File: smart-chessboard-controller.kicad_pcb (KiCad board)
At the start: 4 copper layers, 89.8 x 92.5 mm, 75 parts, among them J1 USB_C_Receptacle_USB2.0, J2 Micro_SD_Card_Det_Hirose_DM3C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, J3 Conn_02x03_Odd_Even, J4 Conn_01x12_MountingPin, J5 NX3224T024, J6 Conn_01x05, J7 Conn_01x05, J8 Conn_01x05, J9 Conn_01x05, Q1 S8050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

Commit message: update USB-C footprint to through hole
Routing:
- net 5V: track 137.6 -> 136.2 mm
- net /W_MOVE: track 38.6 -> 39.7 mm
- net GND: vias 17 -> 26

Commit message: fix pin assignment for black clock connector
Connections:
- J6 pad 2: /SCL_DB -> /SDA_DB
- J6 pad 3: /SDA_DB -> /SCL_DB
- J9 pad 2: /SCL_DBC -> /SDA_DBC
- J9 pad 3: /SDA_DBC -> /SCL_DBC
- R12 pad 2: /SDA_DBC -> /SCL_DBC
- R16 pad 2: /SCL_DBC -> /SDA_DBC
- U5 pad 8: /SCL_DBC -> /SDA_DBC
- U5 pad 9: /SDA_DBC -> /SCL_DBC
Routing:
- net /SDA_DBC: track 21.0 -> 23.4 mm
- net /SCL_DBC: track 23.4 -> 21.0 mm
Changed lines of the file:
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@@
   (title_block
     (title "Smart Chessboard Controller")
-    (date "2022-11-25")
-    (rev "B")
+    (date "2022-12-07")
+    (rev "C")
     (company "Butler Electronics")
   )
@@
       (net 85 "unconnected-(U5-Pad7)") (pinfunction "SC1") (pintype "output+no_connect"))
     (pad "8" smd roundrect (at -2.8625 0.975 90) (size 1.475 0.4) (layers "F.Cu" "F.Paste" "F.Mask") (roundrect_rratio 0.25)
-      (net 99 "/SCL_DBC") (pinfunction "SD2") (pintype "bidirectional"))
+      (net 98 "/SDA_DBC") (pinfunction "SD2") (pintype "bidirectional"))
     (pad "9" smd roundrect (at -2.8625 1.625 90) (size 1.475 0.4) (layers "F.Cu" "F.Paste" "F.Mask") (roundrect_rratio 0.25)
-      (net 98 "/SDA_DBC") (pinfunction "SC2") (pintype "output"))
+      (net 99 "/SCL_DBC") (pinfunction "SC2") (pintype "output"))
     (pad "10" smd roundrect (at -2.8625 2.275 90) (size 1.475 0.4) (layers "F.Cu" "F.Paste" "F.Mask") (roundrect_rratio 0.25)
       (net 96 "/SDA_DWC") (pinfunction "SD3") (pintype "bidirectional"))
@@
       (net 1 "3V3") (pintype "passive"))
     (pad "2" smd roundrect (at 0.825 0 180) (size 0.8 0.95) (layers "F.Cu" "F.Paste" "F.Mask") (roundrect_rratio 0.25)
-      (net 99 "/SCL_DBC") (pintype "passive"))
+      (net 98 "/SDA_DBC") (pintype "passive"))
     (model "${KICAD6_3DMODEL_DIR}/Resistor_SMD.3dshapes/R_0603_1608Metric.wrl"
       (offset (xyz 0 0 0))
@@
       (net 1 "3V3") (pinfunction "Pin_1") (pintype "passive"))
     (pad "2" thru_hole oval (at 2 0) (size 1.2 1.75) (drill 0.75) (layers *.Cu *.Mask)
-      (net 99 "/SCL_DBC") (pinfunction "Pin_2") (pintype "passive"))
+      (net 98 "/SDA_DBC") (pinfunction "Pin_2") (pintype "passive"))
     (pad "3" thru_hole oval (at 4 0) (size 1.2 1.75) (drill 0.75) (layers *.Cu *.Mask)
-      (net 98 "/SDA_DBC") (pinfunction "Pin_3") (pintype "passive"))
+      (net 99 "/SCL_DBC") (pinfunction "Pin_3") (pintype "passive"))
     (pad "4" thru_hole oval (at 6 0) (size 1.2 1.75) (drill 0.75) (layers *.Cu *.Mask)
       (net 38 "/B_MOVE") (pinfunction "Pin_4") (pintype "passive"))
@@
       (net 1 "3V3") (pintype "passive"))
     (pad "2" smd roundrect (at 0.825 0 180) (size 0.8 0.95) (layers "F.Cu" "F.Paste" "F.Mask") (roundrect_rratio 0.25)
-      (net 98 "/SDA_DBC") (pintype "passive"))
+      (net 99 "/SCL_DBC") (pintype "passive"))
     (model "${KICAD6_3DMODEL_DIR}/Resistor_SMD.3dshapes/R_0603_1608Metric.wrl"
       (offset (xyz 0 0 0))
@@
       (net 103 "+3V3") (pinfunction "Pin_1") (pintype "passive"))
     (pad "2" thru_hole oval (at 2 0 180) (size 1.2 1.75) (drill 0.75) (layers *.Cu *.Mask)
-      (net 32 "/SCL_DB") (pinfunction "Pin_2") (pintype "passive"))
+      (net 31 "/SDA_DB") (pinfunction "Pin_2") (pintype "passive"))
     (pad "3" thru_hole oval (at 4 0 180) (size 1.2 1.75) (drill 0.75) (layers *.Cu *.Mask)
-      (net 31 "/SDA_DB") (pinfunction "Pin_3") (pintype "passive"))
+      (net 32 "/SCL_DB") (pinfunction "Pin_3") (pintype "passive"))
     (pad "4" thru_hole oval (at 6 0 180) (size 1.2 1.75) (drill 0.75) (layers *.Cu *.Mask)
       (net 33 "/B_MOVE_BTN") (pinfunction "Pin_4") (pintype "passive"))
@@
   (segment (start 112.52 94.994) (end 108.841 91.315) (width 0.2) (layer "F.Cu") (net 97))
   (segment (start 112.586 89.027) (end 112.268 89.027) (width 0.25) (layer "F.Cu") (net 97))
-  (segment (start 112.586 85.979) (end 109.855 85.979) (width 0.25) (layer "F.Cu") (net 98))
-  (segment (start 107.541 92.103) (end 105.664 93.98) (width 0.25) (layer "F.Cu") (net 98))
-  (segment (start 109.855 85.979) (end 107.541 88.293) (width 0.25) (layer "F.Cu") (net 98))
-  (segment (start 99.312 95.506) (end 99.312 97.08) (width 0.25) (layer "F.Cu") (net 98))
-  (segment (start 107.541 89.6035) (end 107.541 92.103) (width 0.25) (layer "F.Cu") (net 98))
-  (segment (start 100.838 93.98) (end 99.312 95.506) (width 0.25) (layer "F.Cu") (net 98))
-  (segment (start 105.664 93.98) (end 100.838 93.98) (width 0.25) (layer "F.Cu") (net 98))
-  (segment (start 107.541 88.293) (end 107.541 89.6035) (width 0.25) (layer "F.Cu") (net 98))
-  (segment (start 97.312 95.728) (end 97.312 97.08) (width 0.25) (layer "F.Cu") (net 99))
-  (segment (start 112.586 84.455) (end 111.887 84.455) (width 0.25) (layer "F.Cu") (net 99))
-  (segment (start 99.695 93.345) (end 97.312 95.728) (width 0.25) (layer "F.Cu") (net 99))
-  (segment (start 110.81252 85.52948) (end 109.541802 85.52948) (width 0.25) (layer "F.Cu") (net 99))
-  (segment (start 111.887 84.455) (end 110.81252 85.52948) (width 0.25) (layer "F.Cu") (net 99))
-  (segment (start 106.891 88.180282) (end 106.891 89.6035) (width 0.25) (layer "F.Cu") (net 99))
-  (segment (start 105.283 93.345) (end 99.695 93.345) (width 0.25) (layer "F.Cu") (net 99))
-  (segment (start 109.541802 85.52948) (end 106.891 88.180282) (width 0.25) (layer "F.Cu") (net 99))
-  (segment (start 106.891 89.6035) (end 106.891 91.737) (width 0.25) (layer "F.Cu") (net 99))
-  (segment (start 106.891 91.737) (end 105.283 93.345) (width 0.25) (layer "F.Cu") (net 99))
+  (segment (start 112.586 84.455) (end 111.887 84.455) (width 0.25) (layer "F.Cu") (net 98))
+  (segment (start 99.695 93.345) (end 97.312 95.728) (width 0.25) (layer "F.Cu") (net 98))
+  (segment (start 110.81252 85.52948) (end 109.541802 85.52948) (width 0.25) (layer "F.Cu") (net 98))
+  (segment (start 111.887 84.455) (end 110.81252 85.52948) (width 0.25) (layer "F.Cu") (net 98))
+  (segment (start 106.891 88.180282) (end 106.891 89.6035) (width 0.25) (layer "F.Cu") (net 98))
+  (segment (start 105.283 93.345) (end 99.695 93.345) (width 0.25) (layer "F.Cu") (net 98))
+  (segment (start 97.312 95.728) (end 97.312 97.08) (width 0.25) (layer "F.Cu") (net 98))
+  (segment (start 109.541802 85.52948) (end 106.891 88.180282) (width 0.25) (layer "F.Cu") (net 98))
+  (segment (start 106.891 89.6035) (end 106.891 91.737) (width 0.25) (layer "F.Cu") (net 98))
+  (segment (start 106.891 91.737) (end 105.283 93.345) (width 0.25) (layer "F.Cu") (net 98))
+  (segment (start 112.586 85.979) (end 109.855 85.979) (width 0.25) (layer "F.Cu") (net 99))
+  (segment (start 107.541 92.103) (end 105.664 93.98) (width 0.25) (layer "F.Cu") (net 99))
+  (segment (start 109.855 85.979) (end 107.541 88.293) (width 0.25) (layer "F.Cu") (net 99))
+  (segment (start 107.541 89.6035) (end 107.541 92.103) (width 0.25) (layer "F.Cu") (net 99))
+  (segment (start 100.838 93.98) (end 99.312 95.506) (width 0.25) (layer "F.Cu") (net 99))
+  (segment (start 99.312 95.506) (end 99.312 97.08) (width 0.25) (layer "F.Cu") (net 99))
+  (segment (start 105.664 93.98) (end 100.838 93.98) (width 0.25) (layer "F.Cu") (net 99))
+  (segment (start 107.541 88.293) (end 107.541 89.6035) (width 0.25) (layer "F.Cu") (net 99))
   (segment (start 96.022 118.0084) (end 96.652 117.3784) (width 0.25) (layer "B.Cu") (net 103))
   (segment (start 96.652 117.3784) (end 99.412 117.3784) (width 0.25) (layer "B.Cu") (net 103))

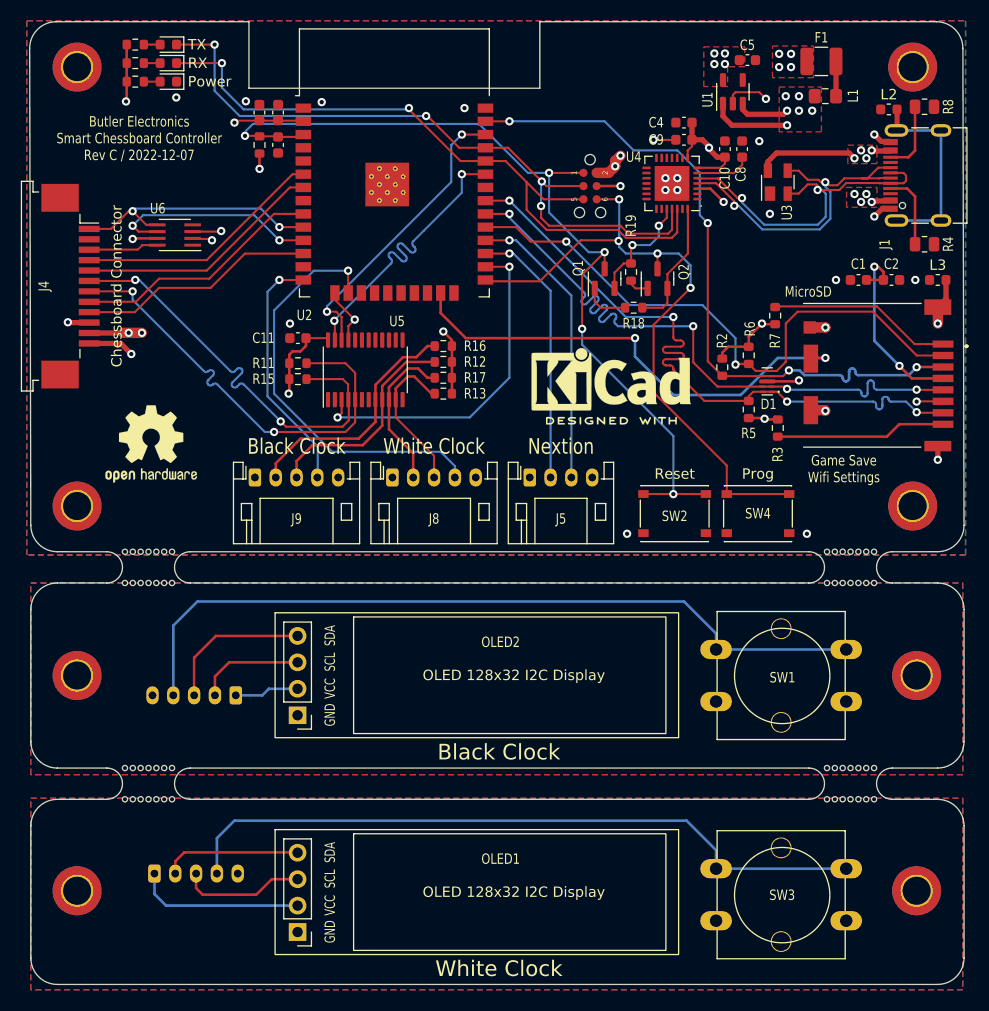
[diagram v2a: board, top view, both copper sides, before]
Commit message: remove chess clock/button
Remove chess clock/buttons from controller design. They were
moved to separate design since it's more expensive to
manufacture boards with panelization. They charge extra if
there are different designs with one gerber file with
panelization.
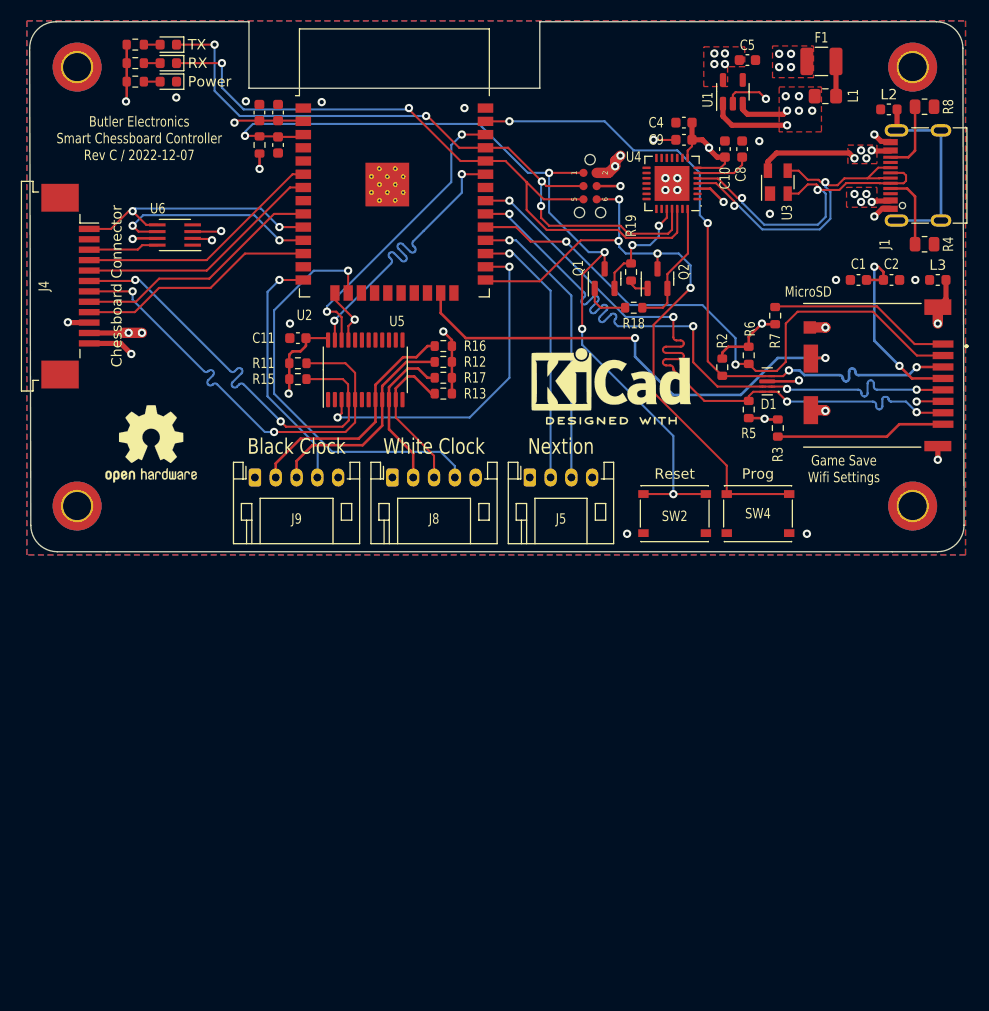
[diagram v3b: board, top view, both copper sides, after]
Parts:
- removed H1, H2, H3, H4: MountingHole, MountingHole:MountingHole_2.7mm_M2.5_DIN965_Pad_TopBottom
- removed J6, J7: Conn_01x05, Connector_JST:JST_PH_S5B-PH-K_1x05_P2.00mm_Horizontal
- removed OLED1, OLED2: OLED_I2C, User Custom Footprint:OLED_128x32_I2C_4pins
- removed SW1, SW3: SW_SPST, User Custom Footprint:Button_SW_12mm_1.8mm_hole
- removed mouse-bite-3mm-slot (x4): VAL**, Panelization:mouse-bite-3mm-slot
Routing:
- net /B_MOVE_BTN: track 75.1 -> 0.00 mm
- net /W_MOVE_BTN: track 67.5 -> 0.00 mm
- net +3.3VA: track 16.2 -> 0.00 mm
- net /SDA_DB: track 14.4 -> 0.00 mm
- net /SDA_DW: track 13.3 -> 0.00 mm
- net /SCL_DW: track 12.0 -> 0.00 mm
- net /SCL_DB: track 10.3 -> 0.00 mm
- net +3V3: track 6.20 -> 0.00 mm
- net /IO0: track 63.5 -> 62.6 mm
- net /D_P: track 32.9 -> 32.4 mm
- removed copper zone on B.Cu, net GND1
- removed copper zone on F.Cu, net GND1
- removed copper zone on In1.Cu, net GND1
- removed copper zone on In2.Cu, net GND1
- removed copper zone on B.Cu, net GND2
- removed copper zone on F.Cu, net GND2
- removed copper zone on In1.Cu, net GND2
- removed copper zone on In2.Cu, net GND2
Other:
- board size 89.8 x 92.5 mm -> 89.8 x 50.9 mm

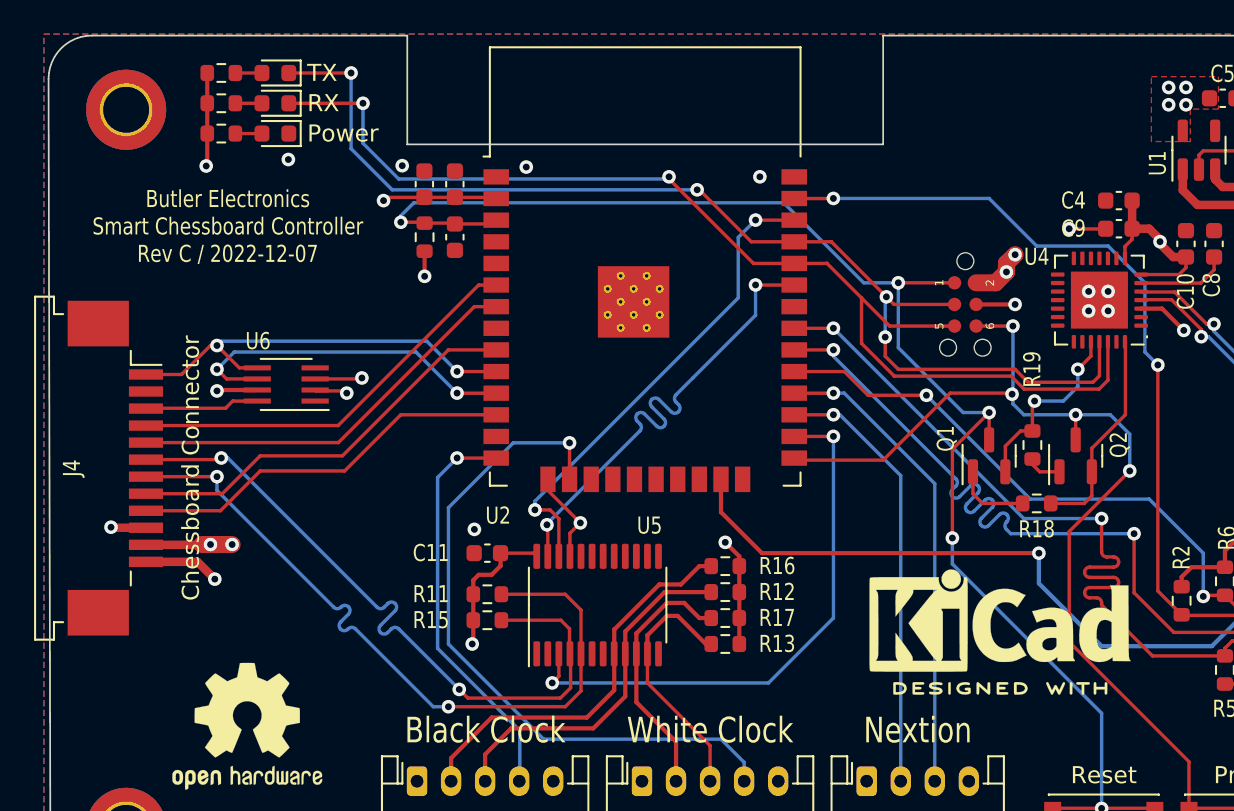
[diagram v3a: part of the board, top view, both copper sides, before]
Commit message: fix issues from rev.B
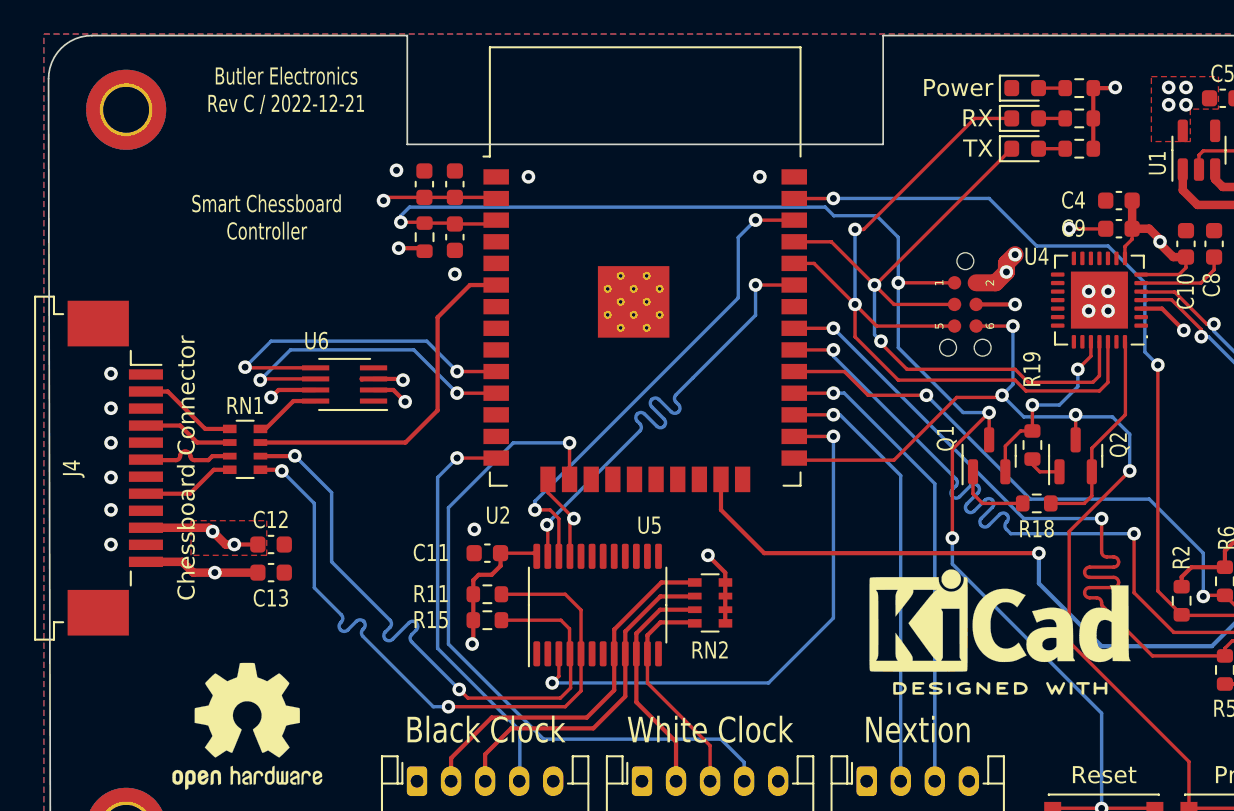
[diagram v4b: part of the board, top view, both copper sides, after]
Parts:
- removed R12, R13, R16, R17: 2K7, Resistor_SMD:R_0603_1608Metric
- added C12: 100nF, Capacitor_SMD:C_0603_1608Metric, F.Cu at (86.7, 83.2)
- added C13: 100nF, Capacitor_SMD:C_0603_1608Metric, F.Cu at (86.7, 84.8)
- added RN1: 33, Resistor_SMD:R_Array_Convex_4x0603, F.Cu at (85.2, 77.6)
- added RN2: 1K, Resistor_SMD:R_Array_Convex_4x0603, F.Cu at (112.5, 86.6)
- R11, R15: value 2K7 -> 1K
- moved R9 50.6 mm to (134.2, 59.9), turned to 180 degrees
- moved R14 50.4 mm to (134.2, 56.4), turned to 180 degrees
- moved R10 50.4 mm to (134.2, 58.2), turned to 180 degrees
- moved LED1 44.2 mm to (131.0, 59.9), turned to 0 degrees
- moved LED3 44.1 mm to (131.0, 56.4), turned to 0 degrees
- moved LED2 44.0 mm to (131.0, 58.2), turned to 0 degrees
- moved U6 3.43 mm to (91.1, 73.8)
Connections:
- J4 pad 1: /LED_IC_3 -> GND
- J4 pad 10: GND -> 5V
- J4 pad 11: 5V -> GND
- J4 pad 2: unconnected-(J4-Pad2) -> Net-(J4-Pad2)
- J4 pad 3: /LED_IC_5 -> GND
- J4 pad 4: /IO_INT0 -> Net-(J4-Pad4)
- J4 pad 5: /IO_INT1 -> GND
- J4 pad 6: ~{SDA_IOMUX} -> Net-(J4-Pad6)
- J4 pad 7: ~{SCL_IOMUX} -> GND
- J4 pad 8: /IO_INT2 -> Net-(J4-Pad8)
- J4 pad 9: /IO_INT3 -> GND
- U2 pad 12: /IO_INT3 -> unconnected-(U2-Pad12)
- U2 pad 6: /IO_INT0 -> /IO_INT
- U2 pad 7: /IO_INT1 -> unconnected-(U2-Pad7)
- U2 pad 9: /IO_INT2 -> unconnected-(U2-Pad9)
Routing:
- net /ESP_TX: track 66.2 -> 41.8 mm, vias 4 -> 2
- net /IO_INT2: track 24.1 -> 0.00 mm
- net /IO_INT0: track 24.0 -> 0.00 mm
- net /IO_INT1: track 23.9 -> 0.00 mm
- net /IO_INT3: track 22.9 -> 0.00 mm
- net /IO_INT: track 0.00 -> 20.9 mm
- net /ESP_RX: track 66.8 -> 47.9 mm
- net 3V3: track 315.0 -> 303.2 mm
- net Net-(J4-Pad2): track 0.00 -> 5.83 mm
- net Net-(J4-Pad6): track 0.00 -> 5.56 mm
- net Net-(J4-Pad8): track 0.00 -> 5.50 mm
- net Net-(J4-Pad4): track 0.00 -> 5.33 mm
- net /LED_IC_3: track 25.0 -> 20.3 mm
- net ~{SCL_IOMUX}: track 43.5 -> 39.5 mm
- net ~{SDA_IOMUX}: track 41.5 -> 37.5 mm
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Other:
- board text added: "${COMPANY} Rev ${REVISION} / ${ISSUE_DATE}"
- board text added: "Smart Chessboard Controller"
- board text removed: "${COMPANY} ${TITLE} Rev ${REVISION} / ${ISSUE_DATE}"
